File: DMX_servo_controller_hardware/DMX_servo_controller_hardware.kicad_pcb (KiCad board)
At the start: 4 copper layers, 0 parts

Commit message: Imports schematic into PCB file and roughly separates components in blocks
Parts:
- added C1: 100nF, Capacitor_SMD:C_0805_2012Metric_Pad1.18x1.45mm_HandSolder, F.Cu at (181.0, 65.0)
- added C10: 1μF, Capacitor_SMD:C_0805_2012Metric_Pad1.18x1.45mm_HandSolder, F.Cu at (136.1, 45.1)
- added C2: 1μF, Capacitor_SMD:C_0805_2012Metric_Pad1.18x1.45mm_HandSolder, F.Cu at (181.0, 68.0)
- added C3: 1000μF, Capacitor_THT:CP_Radial_D10.0mm_P5.00mm, F.Cu at (45.0, 40.0)
- added C4: 100nF, Capacitor_SMD:C_0805_2012Metric_Pad1.18x1.45mm_HandSolder, F.Cu at (49.0, 70.0)
- added C5: 1μF, Capacitor_SMD:C_0805_2012Metric_Pad1.18x1.45mm_HandSolder, F.Cu at (49.0, 75.0)
- added C6: 100nF, Capacitor_SMD:C_0805_2012Metric_Pad1.18x1.45mm_HandSolder, F.Cu at (76.0, 131.0)
- added C7: 1μF, Capacitor_SMD:C_0805_2012Metric_Pad1.18x1.45mm_HandSolder, F.Cu at (55.0, 70.0)
- added C8: 100nF, Capacitor_SMD:C_0805_2012Metric_Pad1.18x1.45mm_HandSolder, F.Cu at (55.0, 75.0)
- added C9: 100nF, Capacitor_SMD:C_0805_2012Metric_Pad1.18x1.45mm_HandSolder, F.Cu at (136.1, 42.1)
- added D1: SM712_SOT23, Package_TO_SOT_SMD:SOT-23, F.Cu at (48.0, 134.0)
- added D2: C211752 M7, Diode_SMD:D_SMA, F.Cu at (139.2, 25.1)
- added H1: MountingHole, MountingHole:MountingHole_4.3mm_M4_ISO7380, F.Cu at (276.0, 18.7)
- added H2: MountingHole, MountingHole:MountingHole_4.3mm_M4_ISO7380, F.Cu at (276.0, 27.9)
- added H3: MountingHole, MountingHole:MountingHole_4.3mm_M4_ISO7380, F.Cu at (276.0, 37.0)
- added H4: MountingHole, MountingHole:MountingHole_4.3mm_M4_ISO7380, F.Cu at (276.0, 46.1)
- added J1: To_XLR3, Connector_JST:JST_XH_B3B-XH-AM_1x03_P2.50mm_Vertical, F.Cu at (45.0, 117.2)
- added J2: To_XLR3, Connector_JST:JST_XH_B3B-XH-AM_1x03_P2.50mm_Vertical, F.Cu at (45.0, 125.0)
- added J3: Power connector, TerminalBlock:TerminalBlock_bornier-2_P5.08mm, F.Cu at (25.0, 39.9)
- added J4: Display, Connector_JST:JST_XH_B4B-XH-AM_1x04_P2.50mm_Vertical, F.Cu at (188.5, 32.0)
- added J5: Rotary encoder, Connector_JST:JST_XH_B5B-XH-AM_1x05_P2.50mm_Vertical, F.Cu at (186.0, 22.0)
- added J6: Output block 1, Connector_JST:JST_XH_B5B-XH-AM_1x05_P2.50mm_Vertical, F.Cu at (215.0, 78.2)
- added J7: Output block 2, Connector_JST:JST_XH_B5B-XH-AM_1x05_P2.50mm_Vertical, F.Cu at (215.0, 86.0)
- added J8: Output block 3, Connector_JST:JST_XH_B5B-XH-AM_1x05_P2.50mm_Vertical, F.Cu at (215.0, 93.8)
- added J9: Output block 4, Connector_JST:JST_XH_B5B-XH-AM_1x05_P2.50mm_Vertical, F.Cu at (215.0, 101.6)
- added PS1: MEE1S0505SC, Converter_DCDC:Converter_DCDC_Murata_MEE1SxxxxSC_THT, F.Cu at (47.5, 65.0)
- added Q1: BSS138, Package_TO_SOT_SMD:SOT-23, F.Cu at (171.9, 78.5)
- added Q2: BSS138, Package_TO_SOT_SMD:SOT-23, F.Cu at (171.9, 83.0)
- added R1: 10kΩ, Resistor_SMD:R_0805_2012Metric_Pad1.20x1.40mm_HandSolder, F.Cu at (163.0, 61.1)
- added R10: 220Ω, Resistor_SMD:R_0805_2012Metric_Pad1.20x1.40mm_HandSolder, F.Cu at (196.0, 73.2)
- added R11: 220Ω, Resistor_SMD:R_0805_2012Metric_Pad1.20x1.40mm_HandSolder, F.Cu at (196.0, 76.1)
- added R12: 220Ω, Resistor_SMD:R_0805_2012Metric_Pad1.20x1.40mm_HandSolder, F.Cu at (196.0, 79.0)
- added R13: 220Ω, Resistor_SMD:R_0805_2012Metric_Pad1.20x1.40mm_HandSolder, F.Cu at (196.0, 82.0)
- added R14: 220Ω, Resistor_SMD:R_0805_2012Metric_Pad1.20x1.40mm_HandSolder, F.Cu at (196.0, 85.0)
- added R15: 220Ω, Resistor_SMD:R_0805_2012Metric_Pad1.20x1.40mm_HandSolder, F.Cu at (196.0, 87.9)
- added R16: 220Ω, Resistor_SMD:R_0805_2012Metric_Pad1.20x1.40mm_HandSolder, F.Cu at (196.0, 90.8)
- added R17: 220Ω, Resistor_SMD:R_0805_2012Metric_Pad1.20x1.40mm_HandSolder, F.Cu at (200.8, 70.2)
- added R18: 220Ω, Resistor_SMD:R_0805_2012Metric_Pad1.20x1.40mm_HandSolder, F.Cu at (200.8, 73.2)
- added R19: 220Ω, Resistor_SMD:R_0805_2012Metric_Pad1.20x1.40mm_HandSolder, F.Cu at (200.8, 76.1)
- added R2: 10kΩ, Resistor_SMD:R_0805_2012Metric_Pad1.20x1.40mm_HandSolder, F.Cu at (163.0, 64.1)
- added R20: 220Ω, Resistor_SMD:R_0805_2012Metric_Pad1.20x1.40mm_HandSolder, F.Cu at (200.8, 79.0)
- added R21: 220Ω, Resistor_SMD:R_0805_2012Metric_Pad1.20x1.40mm_HandSolder, F.Cu at (200.8, 82.0)
- added R22: 220Ω, Resistor_SMD:R_0805_2012Metric_Pad1.20x1.40mm_HandSolder, F.Cu at (200.8, 85.0)
- added R23: 220Ω, Resistor_SMD:R_0805_2012Metric_Pad1.20x1.40mm_HandSolder, F.Cu at (200.8, 87.9)
- added R24: 220Ω, Resistor_SMD:R_0805_2012Metric_Pad1.20x1.40mm_HandSolder, F.Cu at (200.8, 90.8)
- added R25: 220Ω, Resistor_SMD:R_0805_2012Metric_Pad1.20x1.40mm_HandSolder, F.Cu at (205.5, 70.2)
- added R26: 470Ω, Resistor_SMD:R_0805_2012Metric_Pad1.20x1.40mm_HandSolder, F.Cu at (85.0, 131.0)
- added R27: 330Ω, Resistor_SMD:R_0805_2012Metric_Pad1.20x1.40mm_HandSolder, F.Cu at (85.0, 134.0)
- added R28: 10kΩ, Resistor_SMD:R_0805_2012Metric_Pad1.20x1.40mm_HandSolder, F.Cu at (146.2, 51.1)
- added R3: 10kΩ, Resistor_SMD:R_0805_2012Metric_Pad1.20x1.40mm_HandSolder, F.Cu at (163.0, 67.0)
- added R4: 10kΩ, Resistor_SMD:R_0805_2012Metric_Pad1.20x1.40mm_HandSolder, F.Cu at (163.0, 70.0)
- added R5: 10kΩ, Resistor_SMD:R_0805_2012Metric_Pad1.20x1.40mm_HandSolder, F.Cu at (163.0, 73.0)
- added R6: 0Ω, Resistor_SMD:R_0805_2012Metric_Pad1.20x1.40mm_HandSolder, F.Cu at (61.0, 131.1)
- added R7: 0Ω, Resistor_SMD:R_0805_2012Metric_Pad1.20x1.40mm_HandSolder, F.Cu at (61.0, 134.0)
- added R8: 680Ω, Resistor_SMD:R_0805_2012Metric_Pad1.20x1.40mm_HandSolder, F.Cu at (61.0, 137.0)
- added R9: 680Ω, Resistor_SMD:R_0805_2012Metric_Pad1.20x1.40mm_HandSolder, F.Cu at (61.0, 140.0)
- added SW1: Reset, Button_Switch_SMD:SW_SPST_TL3342, F.Cu at (138.2, 53.1)
- added U1: PCA9685PW, Package_SO:TSSOP-28_4.4x9.7mm_P0.65mm, F.Cu at (181.1, 77.9)
- added U2: SN65HVD11HD, Package_DIP:DIP-8_W7.62mm, F.Cu at (60.0, 117.4)
- added U3: 6N137, DMX_servo_controller_hardware:6N137-X007T, F.Cu at (80.2, 121.2)
- added U4: Pico, RPi_Pico:RPi_Pico_SMD_TH, F.Cu at (117.2, 49.1)

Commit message: Regroups components in PCB
This is still far from a final positioning, but the groups are more
coherent now.
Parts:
- moved H1 186.8 mm to (102.0, 86.7)
- moved H2 186.8 mm to (102.0, 95.8)
- moved H3 186.8 mm to (102.0, 105.0)
- moved H4 186.8 mm to (102.0, 114.2)
- moved J1 175.6 mm to (196.0, 27.5)
- moved D1 175.4 mm to (193.1, 35.4), turned to -90 degrees
- moved J2 170.2 mm to (184.5, 27.5)
- moved R6 160.6 mm to (195.0, 42.5), turned to -90 degrees
- moved R7 159.0 mm to (191.0, 42.5), turned to -90 degrees
- moved R8 145.3 mm to (182.0, 56.5), turned to -90 degrees
- moved U2 144.9 mm to (194.0, 62.1), turned to 180 degrees
- moved R9 144.8 mm to (182.0, 60.5), turned to -90 degrees
- moved R26 127.7 mm to (198.0, 71.5), turned to 90 degrees
- moved U3 119.3 mm to (190.0, 74.5), turned to 180 degrees
- moved C6 117.8 mm to (182.0, 79.5), turned to -90 degrees
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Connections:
- C1 pad 1: +3.3V -> +5V
- C2 pad 1: +3.3V -> +5V

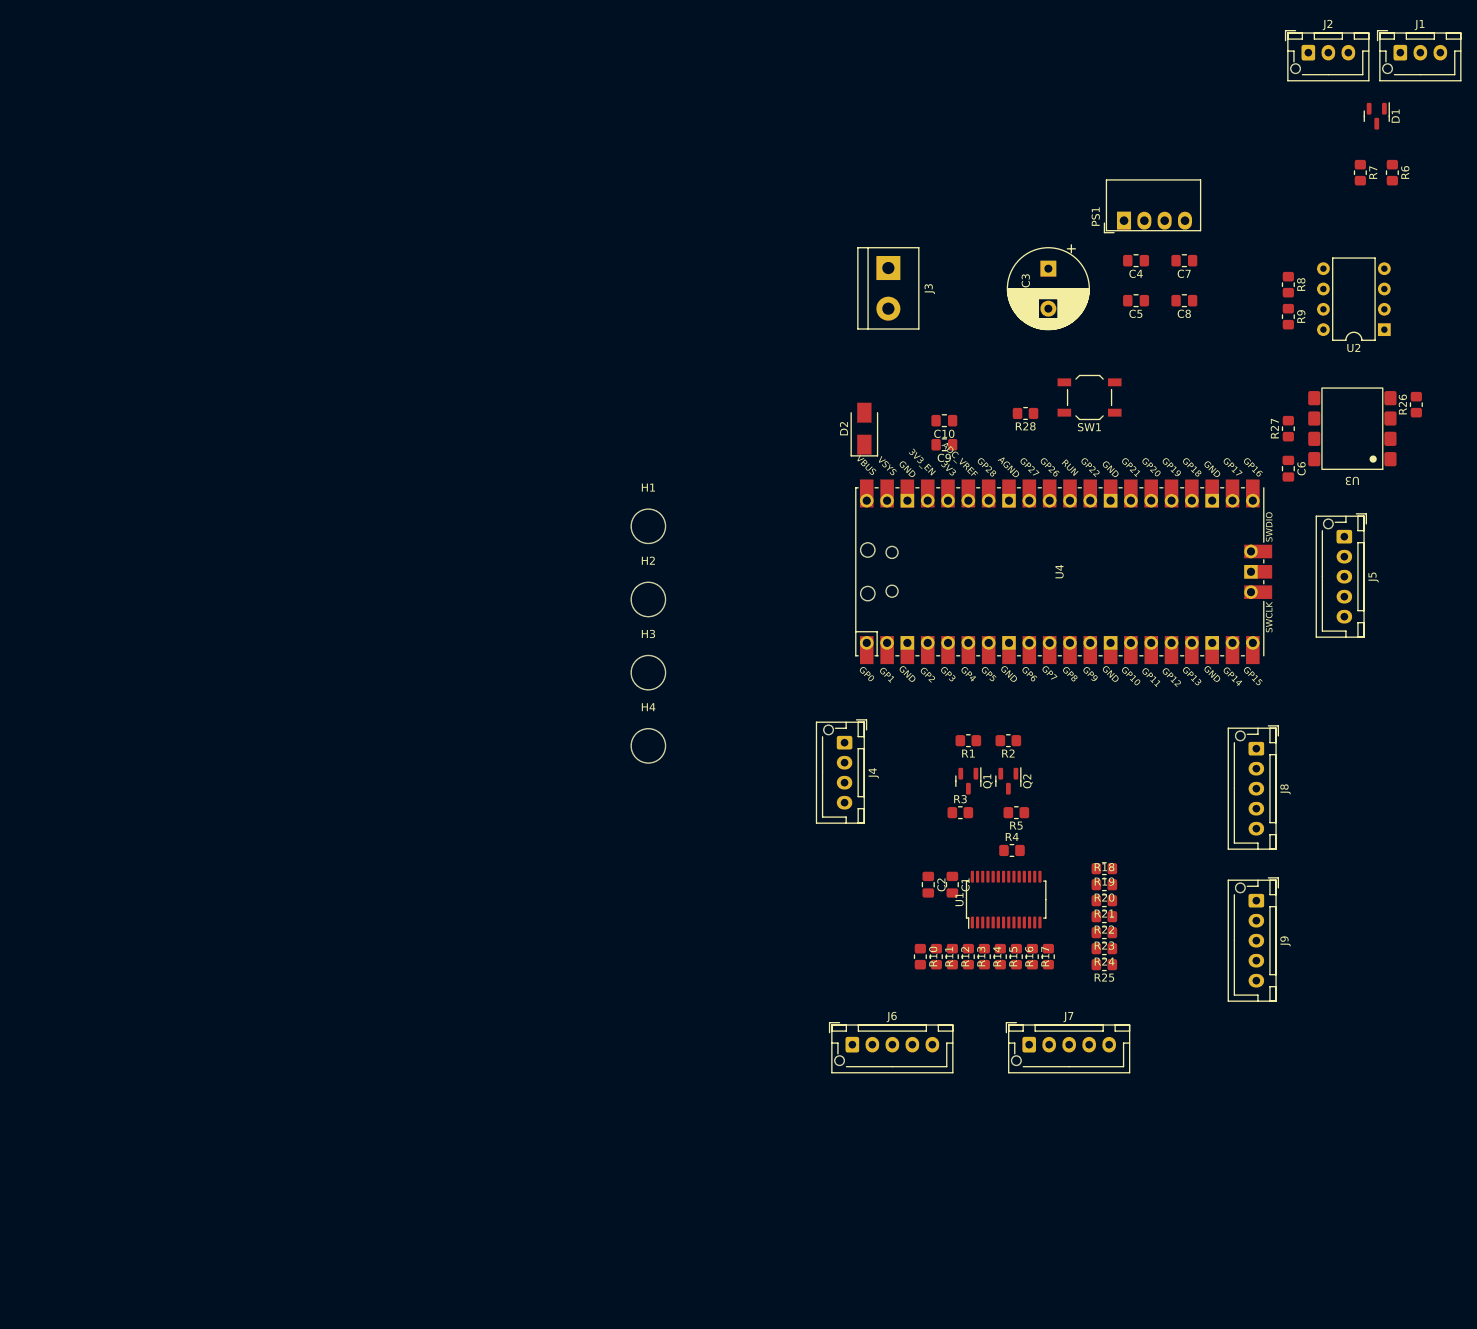
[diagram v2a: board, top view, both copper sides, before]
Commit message: First draft routing of the DMX section of the PCB
This is far from the final layout, but it might help to start
visualizing things.
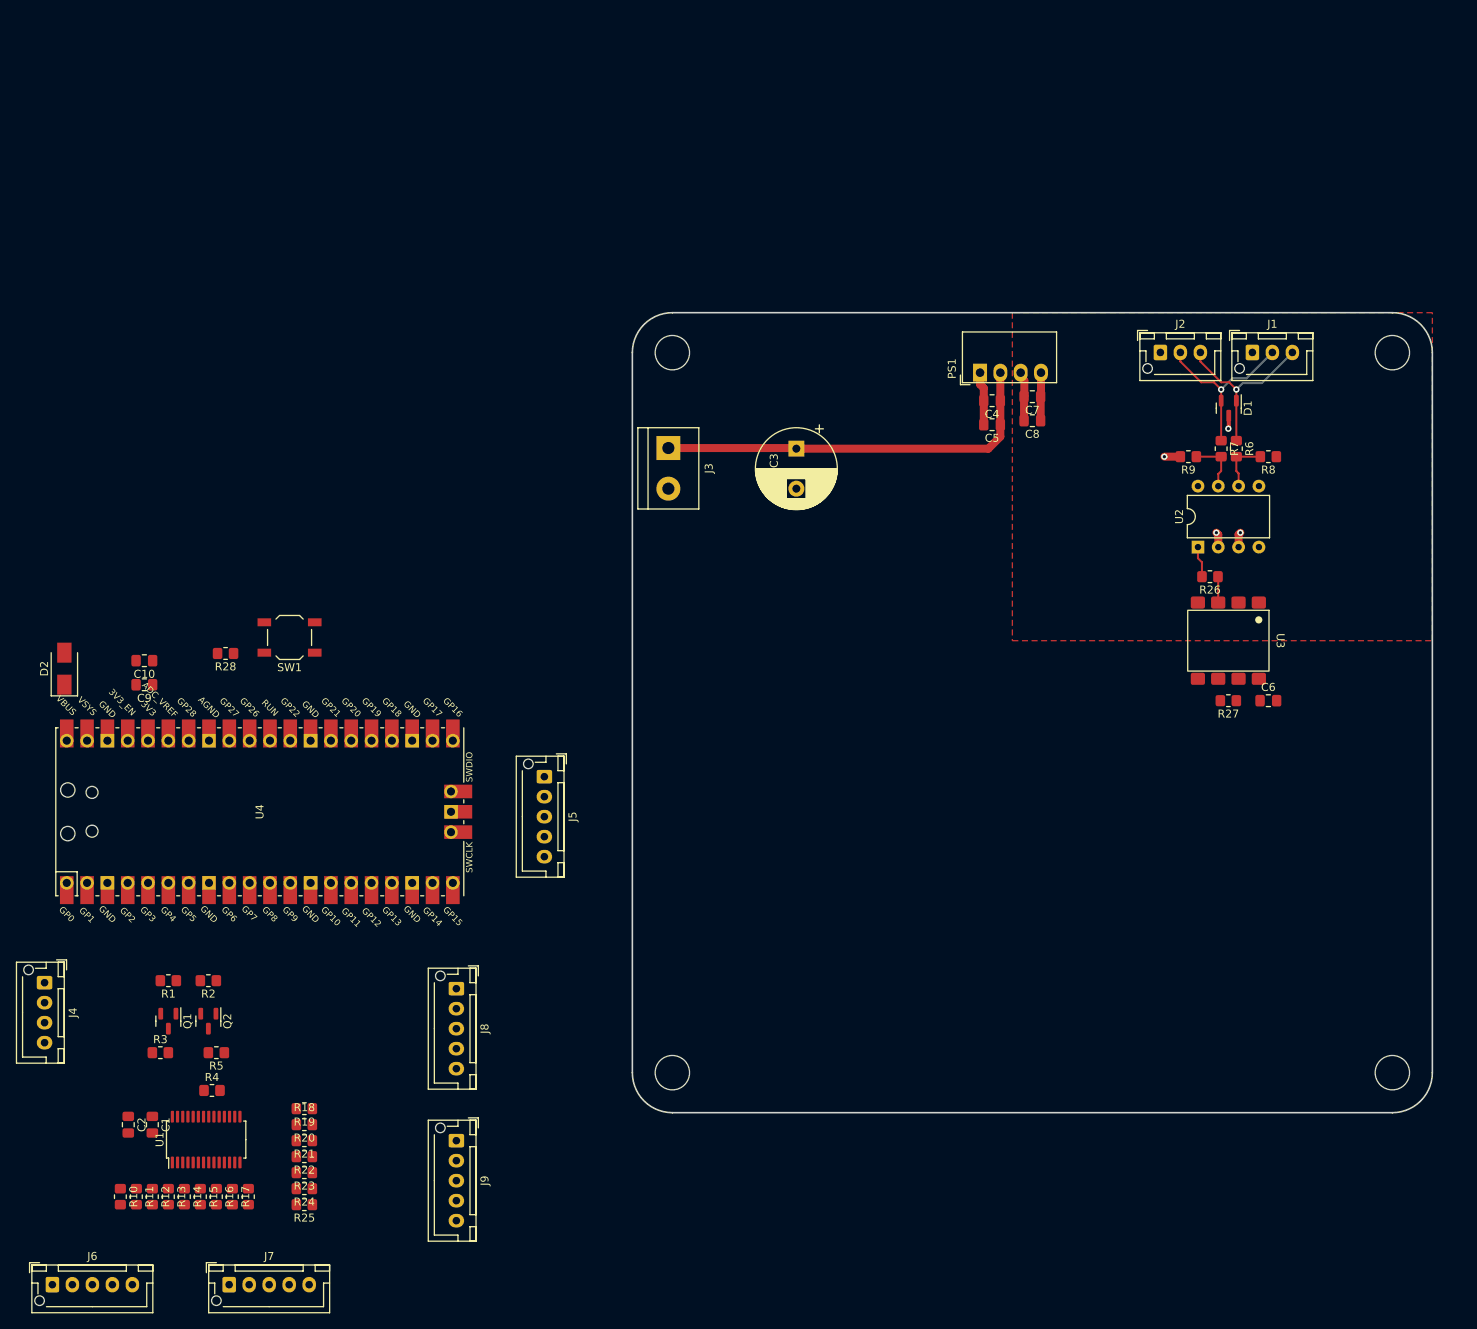
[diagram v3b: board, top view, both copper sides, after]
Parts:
- moved C1 104.4 mm to (40.0, 161.5)
- moved C10 104.4 mm to (39.0, 103.5)
- moved C2 104.4 mm to (37.0, 161.5)
- moved C9 104.4 mm to (39.0, 106.5)
- moved D2 104.4 mm to (29.0, 104.5)
- moved J4 104.4 mm to (26.5, 143.8)
- moved J5 104.4 mm to (89.0, 118.0)
- moved J6 104.4 mm to (27.5, 181.5)
- moved J7 104.4 mm to (49.6, 181.5)
- moved J8 104.4 mm to (78.0, 144.5)
- moved J9 104.4 mm to (78.0, 163.5)
- moved Q1 104.4 mm to (42.0, 148.6)
- moved Q2 104.4 mm to (47.0, 148.6)
- moved R1 104.4 mm to (42.0, 143.5)
- moved R10 104.4 mm to (36.0, 170.5)
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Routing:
- net +5V: track 0.00 -> 50.2 mm
- net DMX_negative/cold: track 0.00 -> 22.4 mm, vias 0 -> 1
- net DMX_positive/hot: track 0.00 -> 22.4 mm, vias 0 -> 1
- net GNDA: track 0.00 -> 13.6 mm, vias 0 -> 4
- net Net-(U2-B): track 0.00 -> 6.93 mm
- net Net-(U2-A): track 0.00 -> 6.80 mm
- net GND: track 0.00 -> 6.69 mm
- net +5VA: track 0.00 -> 6.02 mm
- net Net-(U2-R): track 0.00 -> 3.91 mm
- net Net-(U3-C): track 0.00 -> 3.25 mm
- added copper zone on F.Cu, net +5VA
- added copper zone on In1.Cu, net GNDA
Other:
- board outline added: 100 x 100 mm
